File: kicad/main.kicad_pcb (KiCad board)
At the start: 4 copper layers, 82.3 x 27 mm, 25 parts, among them J1 Barrel_Jack, Q1 Q_NJFET_DGS, Q10 Q_NJFET_GSD, Q11 Q_NJFET_SDG, Q12 Q_NJFET_SGD, Q2 Q_NJFET_DSG, Q3 Q_NJFET_GDS, Q4 Q_NJFET_GSD, Q5 Q_NJFET_SDG, Q6 Q_NJFET_SGD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

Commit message: added qrcode
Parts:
- added G***: LOGO, LOGO, B.Cu at (141.3, 79.1)

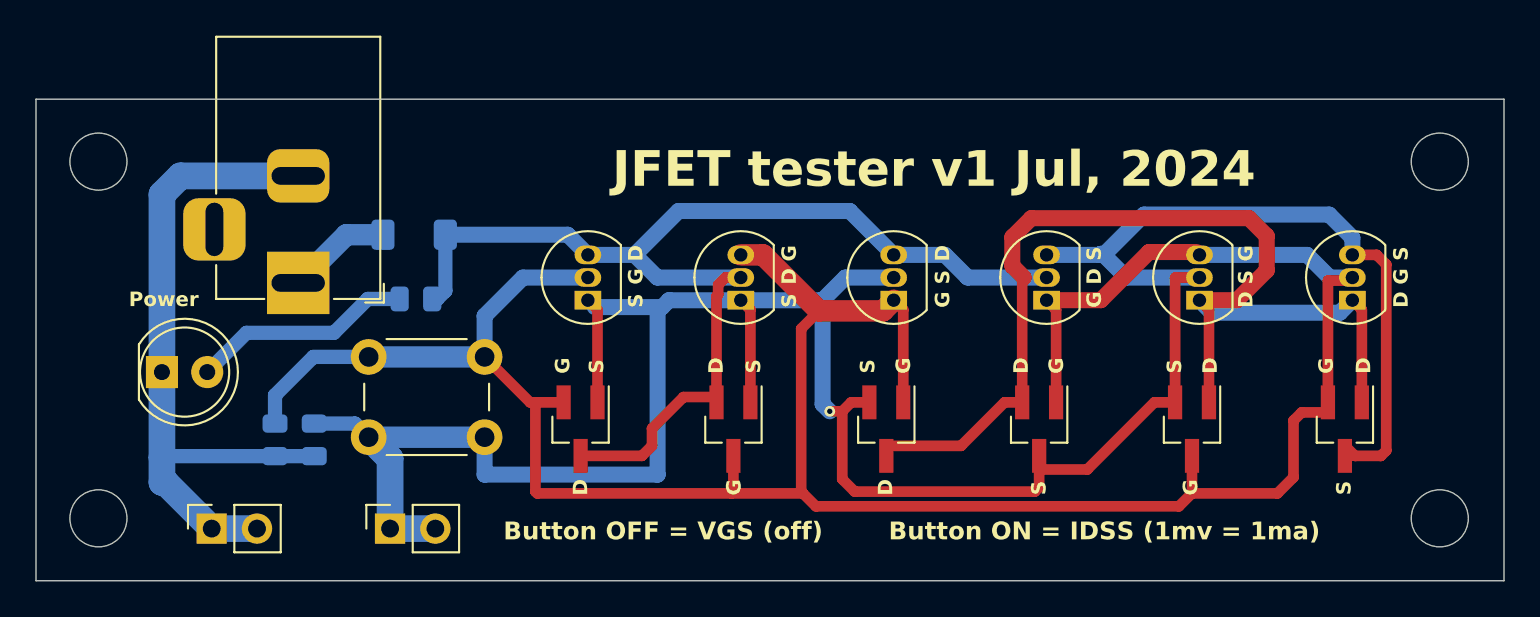
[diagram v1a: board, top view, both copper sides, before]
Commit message: wider pinout
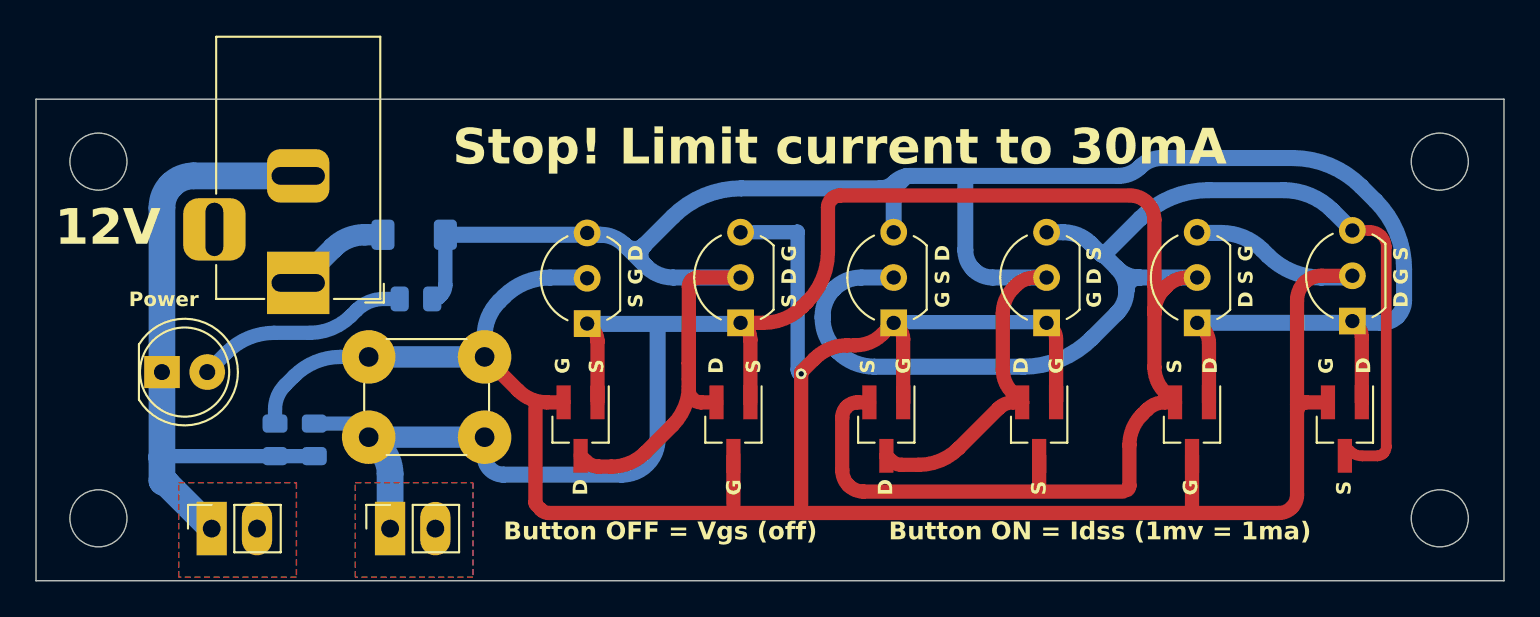
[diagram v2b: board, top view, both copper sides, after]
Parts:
- Q1, Q2, Q3, Q4, Q5, Q6: footprint Package_TO_SOT_THT:TO-92_Inline -> Package_TO_SOT_THT:TO-92_Inline_Wide
- moved Q6 1.31 mm to (111.2, 78.3)
- moved Q2 1.28 mm to (145.4, 78.2)
- moved Q5 1.27 mm to (119.8, 78.2)
- moved Q3 1.27 mm to (137.0, 78.2)
- moved Q4 1.27 mm to (128.4, 78.2)
- moved Q1 1.17 mm to (154.1, 78.1)
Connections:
- TP1 pad 2: DMM+ -> (no net)
- TP2 pad 2: DMM- -> (no net)
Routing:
- net DMM+: track 154.3 -> 194.1 mm, vias 1 -> 0
- net +12V: track 126.4 -> 148.3 mm
- net Net-(Q1-G): track 147.2 -> 151.3 mm, vias 0 -> 1
- net DMM-: track 39.2 -> 36.5 mm
- added copper zone on B.Cu, net DMM+
- added copper zone on F.Cu, net DMM+
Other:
- board text added: "12V"
- board text added: "Button OFF = Vgs (off)"
- board text added: "Button ON = Idss (1mv = 1ma)"
- board text added: "JFET tester v2 Jul, 2024"
- board text added: "Stop! Limit current to 30mA"
- board text removed: "Button OFF = VGS (off)"
- board text removed: "Button ON = IDSS (1mv = 1ma)"
- board text removed: "JFET tester v1 Jul, 2024"
